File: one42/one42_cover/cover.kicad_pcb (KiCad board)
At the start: 2 copper layers, 37.6 x 85.7 mm, 1 part

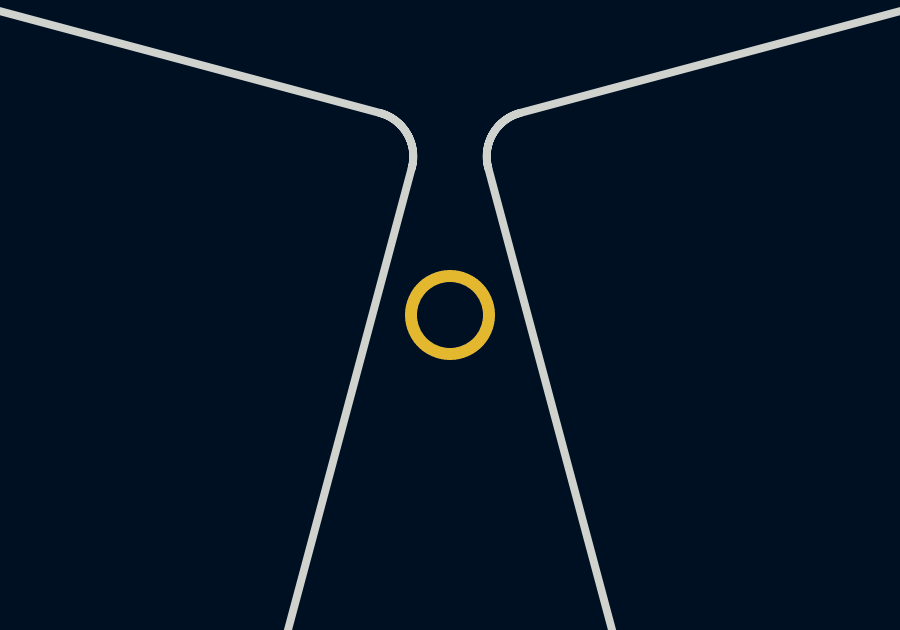
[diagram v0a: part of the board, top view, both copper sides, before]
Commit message: [one42] relocate kicad-project-footprint lib
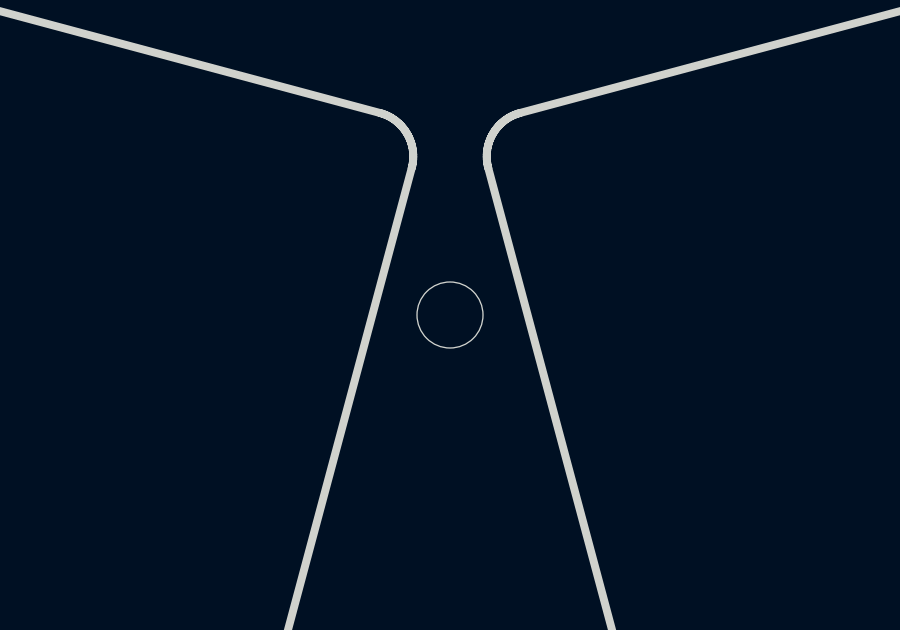
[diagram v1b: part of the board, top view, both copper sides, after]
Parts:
- REF**: footprint one42:one42cover -> one42:one42_cover
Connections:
- REF** pad : shield -> (no net)
